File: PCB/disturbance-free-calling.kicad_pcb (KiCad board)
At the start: 2 copper layers, 74.5 x 20 mm, 22 parts, among them U1 MOUDLE-SEEEDUINO-XIAO-ESP32C3

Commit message: Convert to use ground plane
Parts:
- moved R1 2.56 mm to (136.0, 67.7), turned to 0 degrees
- moved C1 2.54 mm to (136.1, 57.7)
- moved C3 2.54 mm to (121.7, 57.7)
- moved C4 2.54 mm to (114.5, 57.7)
- moved C5 2.54 mm to (107.4, 57.7)
- moved C9 2.54 mm to (78.5, 57.7)
- moved D1 2.54 mm to (135.3, 62.6)
- moved D2 2.54 mm to (128.1, 62.6)
- moved D3 2.54 mm to (120.8, 62.6)
- moved D7 2.54 mm to (92.0, 62.6)
- moved D8 2.54 mm to (84.8, 62.6)
- moved C10 2.54 mm to (71.4, 57.7)
- moved C6 2.54 mm to (100.1, 57.7)
- moved C7 2.54 mm to (92.9, 57.7)
- moved C8 2.54 mm to (85.8, 57.7)
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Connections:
- R1 pad 1: DATA -> Net-(U1-PA6_A10_D10_MOSI)
- R1 pad 2: Net-(U1-PA02_A0_D0) -> DATA
- U1 pad 1: Net-(U1-PA02_A0_D0) -> unconnected-(U1-PA02_A0_D0-Pad1)
- U1 pad 11: unconnected-(U1-PA6_A10_D10_MOSI-Pad11) -> Net-(U1-PA6_A10_D10_MOSI)
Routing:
- net GND: track 168.2 -> 5.97 mm
- net Net-(U1-PA6_A10_D10_MOSI): track 0.00 -> 18.0 mm, vias 0 -> 1
- net Net-(U1-PA02_A0_D0): track 3.63 -> 0.00 mm, vias 1 -> 0
- added copper zone on B.Cu, net GND
- added copper zone on F.Cu, net GND
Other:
- board text added: "ImSeanConroy/Disturbance-Free-Calling (v0.1)"

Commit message: Rearrange layout
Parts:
- U1: footprint xiao ESP32C3_PCB:MOUDLE14P-SMD-2.54-21X17.8MM -> MOUDLE-SEEEDUINO-XIAO-ESP32C3:MOUDLE14P-SMD-2.54-21X17.8MM
- moved R1 2.25 mm to (135.9, 70.0)
- moved U1 1.65 mm to (116.5, 72.5)
- moved D1 1.01 mm to (135.6, 63.5)
- moved D10 1.01 mm to (70.7, 63.5)
- moved D2 1.01 mm to (128.4, 63.5)
- moved D3 1.01 mm to (121.2, 63.5)
- moved D4 1.01 mm to (114.0, 63.5)
- moved D5 1.01 mm to (106.8, 63.5)
- moved D6 1.01 mm to (99.6, 63.5)
- moved D7 1.01 mm to (92.4, 63.5)
- moved D8 1.01 mm to (85.2, 63.5)
- moved D9 1.01 mm to (77.9, 63.5)
- moved C2 0.33 mm to (129.2, 57.5)
- moved C3 0.31 mm to (121.9, 57.5)
- moved C7 0.29 mm to (93.1, 57.5)
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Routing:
- net +5V: track 101.9 -> 116.3 mm
- net GND: track 5.97 -> 0.00 mm, vias 1 -> 4
- net Net-(U1-PA6_A10_D10_MOSI): track 18.0 -> 20.1 mm
- net DATA: track 2.88 -> 4.18 mm
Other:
- board size 74.5 x 20 mm -> 72.5 x 20 mm
- board text added: "ImSeanConroy/Disturbance-Free-Calling (v0.2)"
- board text removed: "ImSeanConroy/Disturbance-Free-Calling (v0.1)"

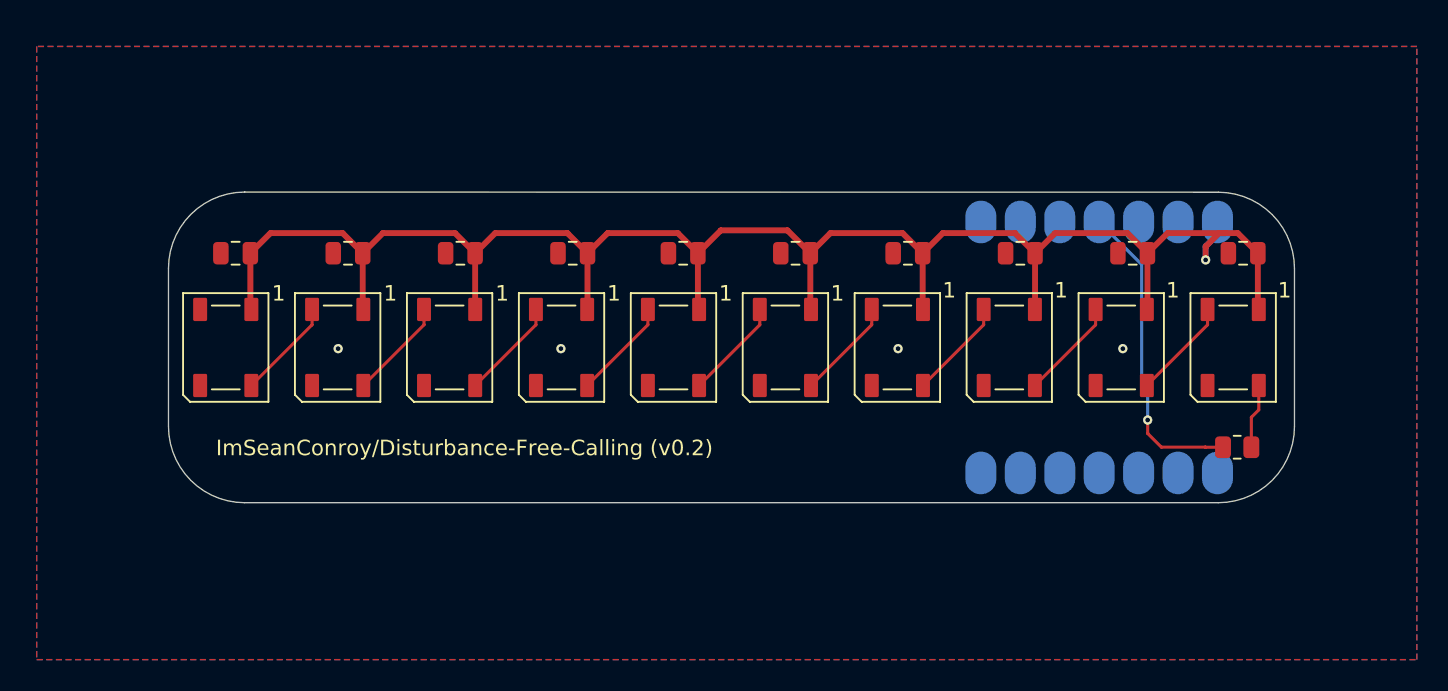
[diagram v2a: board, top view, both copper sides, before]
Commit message: Add mounting holes
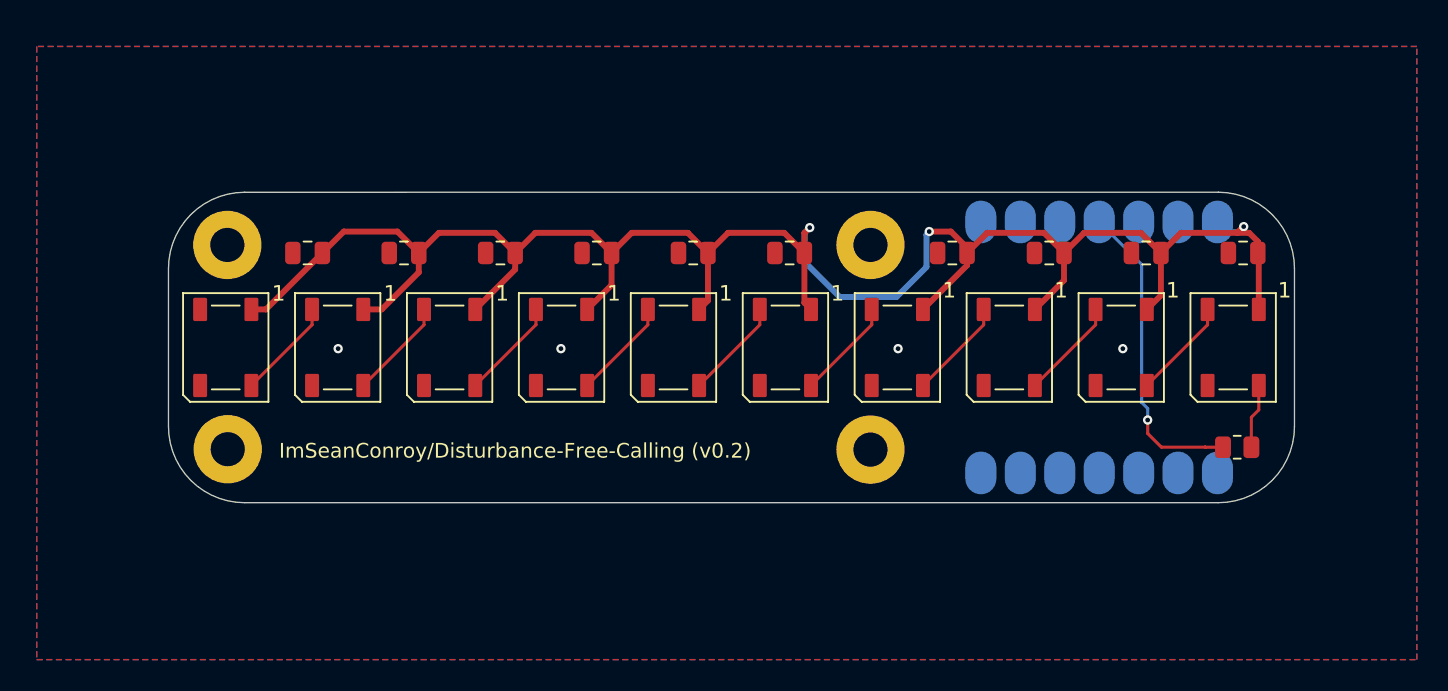
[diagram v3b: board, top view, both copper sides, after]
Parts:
- added H1: MountingHole, MountingHole:MountingHole_2.2mm_M2_Pad, F.Cu at (70.8, 56.9)
- added H2: MountingHole, MountingHole:MountingHole_2.2mm_M2_Pad, F.Cu at (70.9, 70.1)
- added H3: MountingHole, MountingHole:MountingHole_2.2mm_M2_Pad, F.Cu at (112.3, 56.9)
- added H4: MountingHole, MountingHole:MountingHole_2.2mm_M2_Pad, F.Cu at (112.3, 70.1)
- moved C10 4.64 mm to (76.0, 57.5)
- moved C9 3.61 mm to (82.2, 57.5)
- moved C4 2.86 mm to (117.5, 57.5)
- moved C8 2.58 mm to (88.4, 57.5)
- moved C3 1.86 mm to (123.8, 57.5)
- moved C7 1.55 mm to (94.6, 57.5)
- moved C2 0.87 mm to (130.0, 57.5)
- moved C6 0.65 mm to (100.9, 57.5)
- moved C5 0.38 mm to (107.1, 57.5)
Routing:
- net +5V: track 116.3 -> 127.3 mm, vias 1 -> 3
